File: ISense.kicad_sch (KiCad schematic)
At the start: 9 parts, among them U8 INA241A2xDDF

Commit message: added license and almost ready for prod
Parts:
- C46: Rating (none) -> 6.3V
- C48, C50, C52: Rating (none) -> 100V
- C49: Rating (none) -> 5V
- R22, R27: Rating (none) -> 100mW
- R23: Rating (none) -> 6W
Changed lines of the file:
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@@
+			)
+		)
+		(property "Rating" "6.3V"
+			(at 81.28 83.82 0)
+			(effects
+				(font
+					(size 1.27 1.27)
+				)
+				(hide yes)
 			)
 		)
@@
 			)
 		)
+		(property "Rating" "100V"
+			(at 99.06 62.23 0)
+			(effects
+				(font
+					(size 1.27 1.27)
+				)
+				(hide yes)
+			)
+		)
 		(pin "1"
 		)
@@
 			)
 		)
+		(property "Rating" "5V"
+			(at 106.68 62.23 0)
+			(effects
+				(font
+					(size 1.27 1.27)
+				)
+				(hide yes)
+			)
+		)
 		(pin "1"
 		)
@@
 			)
 		)
+		(property "Rating" "100mW"
+			(at 101.6 55.88 0)
+			(effects
+				(font
+					(size 1.27 1.27)
+				)
+				(hide yes)
+			)
+		)
 		(pin "1"
 		)
@@
 		)
 		(property "Description" "Unpolarized capacitor, small symbol"
+			(at 114.3 62.23 0)
+			(effects
+				(font
+					(size 1.27 1.27)
+				)
+				(hide yes)
+			)
+		)
+		(property "Rating" "100V"
 			(at 114.3 62.23 0)
 			(effects
@@
 			)
 		)
+		(property "Rating" "100V"
+			(at 87.63 83.82 0)
+			(effects
+				(font
+					(size 1.27 1.27)
+				)
+				(hide yes)
+			)
+		)
 		(pin "1"
 		)
@@
 			)
 		)
+		(property "Rating" "6W"
+			(at 106.68 40.64 0)
+			(effects
+				(font
+					(size 1.27 1.27)
+				)
+				(hide yes)
+			)
+		)
 		(pin "2"
 		)
@@
 			)
 		)
+		(property "Rating" "100mW"
+			(at 111.76 55.88 0)
+			(effects
+				(font
+					(size 1.27 1.27)
+				)
+				(hide yes)
+			)
+		)
 		(pin "1"
 		)
@@
 			(at 106.68 81.28 0)
 			(effects
+				(font
+					(size 1.27 1.27)
+				)
+				(hide yes)
+			)
+		)
+		(property "Rating" ""
+			(at 106.68 81.28 0)
+			(effects

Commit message: first fab run
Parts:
- removed C46: 4.7uF, Capacitor_SMD:C_0603_1608Metric, symbol Device:C_Small
- added C4: 4.7uF, Capacitor_SMD:C_0603_1608Metric, symbol Device:C
- C48, C50: Manufacturer_Part_Number (none) -> CGA0603X7R104K101JT; Source (none) -> LCSC
- C49: Manufacturer_Part_Number (none) -> CSA0603X7R103K500JT; Source (none) -> LCSC
- C52: Manufacturer_Part_Number (none) -> CGA0603X7R104K500JT; Rating 100V -> 6.3V; Source (none) -> LCSC
- R22, R27: Manufacturer_Part_Number (none) -> RTT0310R0FTP; Source (none) -> LCSC
- R23: Manufacturer_Part_Number (none) -> ASR-M-3-0.5F; Source (none) -> LCSC
- U8: value INA241A2xDDF -> INA240A2; footprint Package_TO_SOT_SMD:SOT-23-8 -> Package_SO:SO-8_3.9x4.9mm_P1.27mm; Manufacturer_Part_Number (none) -> INA240A2DR; Rating (none) -> 80V; Source (none) -> LCSC
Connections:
- net GND: now also C4.2
- net V_{DDA}: now also C4.1
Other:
- note added: "Common Mode Low Pass at 16kHz"
- note added: "Current Sense Shunt Resistor"
- note added: "Differential Low Pass at 800 kHz"
- note added: "I_{MAX} = 66A, I_{MIN} = -66A, V_{DDA} = 3.3V"
- note added: "V_{SENSE} = V_{DDA}/2 + I_{SHUNT} * .025"

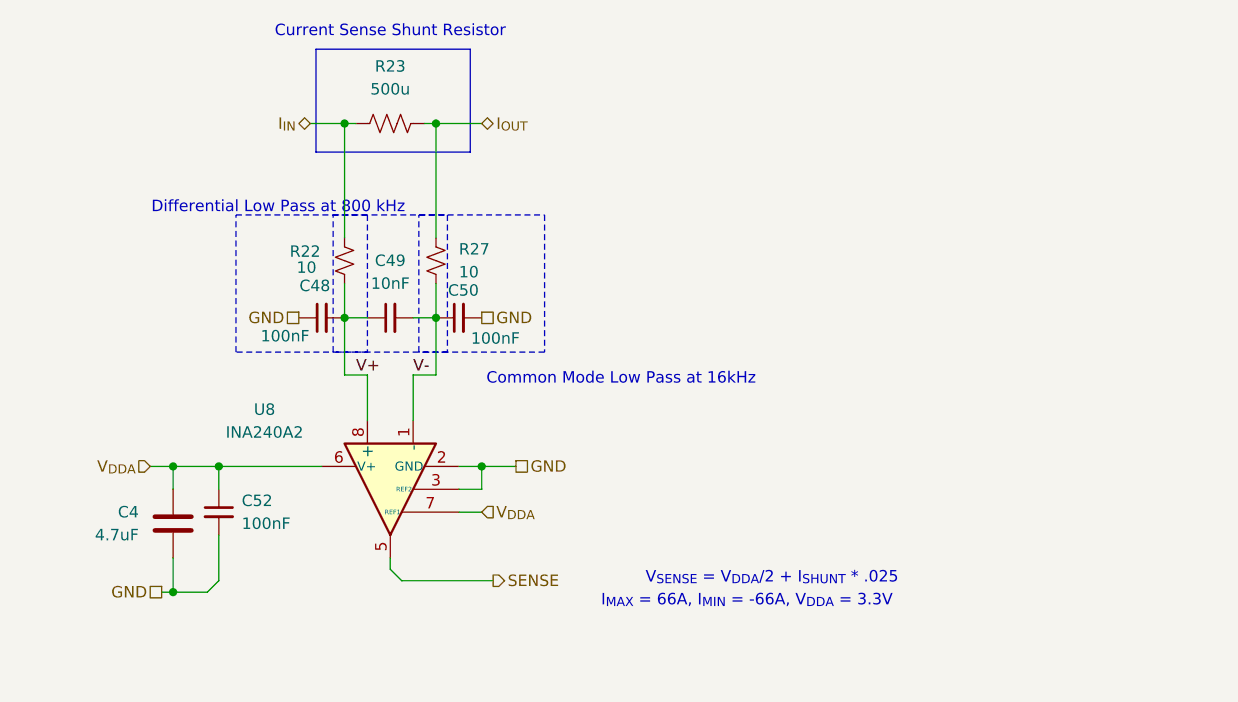
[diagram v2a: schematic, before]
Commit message: added ESD protection
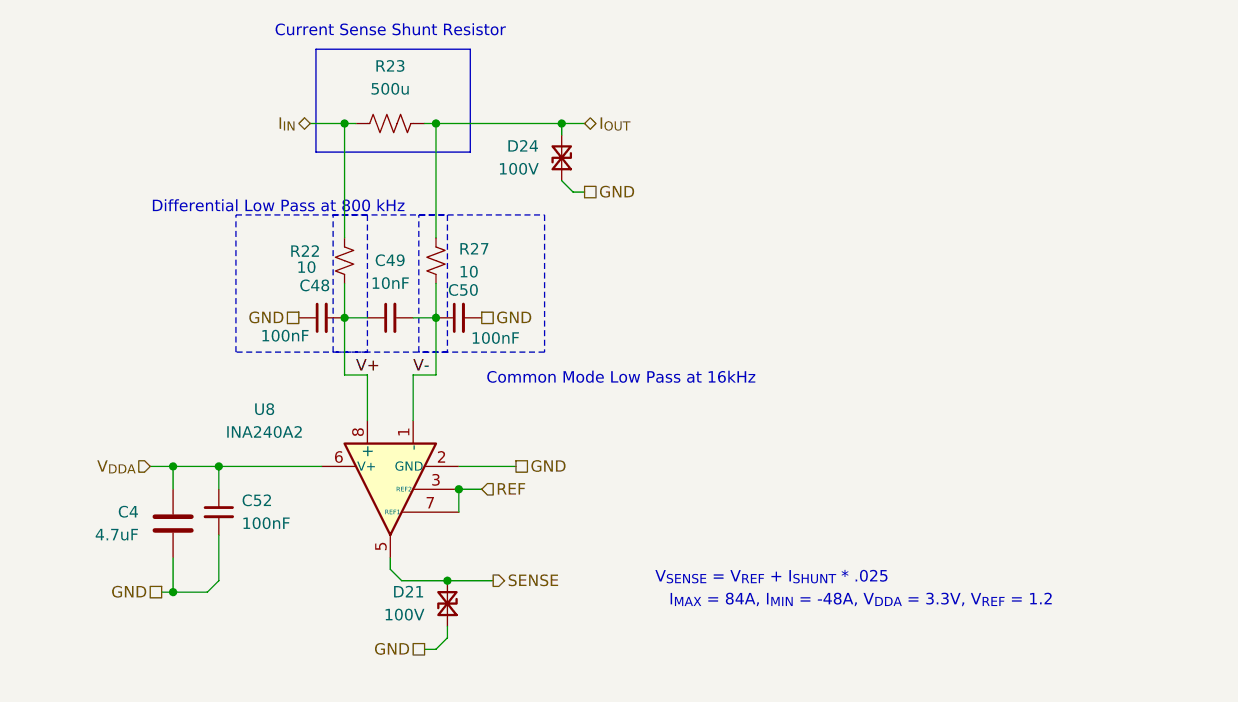
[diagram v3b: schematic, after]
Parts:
- added D21, D24: 100V, Diode_SMD:D_0603_1608Metric, symbol Device:D_TVS_Small
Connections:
- net GND: now also D21.1 (A1), D24.1 (A1); no longer U8.3 (REF2)
- net I_{OUT}: now also D24.2 (A2)
- net SENSE: now also D21.2 (A2)
- net V_{DDA}: no longer U8.7 (REF1)
- new net REF: U8.3 (REF2), U8.7 (REF1)
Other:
- note added: "I_{MAX} = 84A, I_{MIN} = -48A, V_{DDA} = 3.3V, V_{REF} = 1.2"
- note added: "V_{SENSE} = V_{REF} + I_{SHUNT} * .025"
- note removed: "I_{MAX} = 66A, I_{MIN} = -66A, V_{DDA} = 3.3V"
- note removed: "V_{SENSE} = V_{DDA}/2 + I_{SHUNT} * .025"

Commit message: add context
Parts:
- R23: value 500u -> .3m; Rating 6W -> 3W
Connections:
- net GND: now also U8.3 (REF2)
- net V_{DDA}: now also U8.7 (REF1)
- removed net REF: U8.3 (REF2), U8.7 (REF1)
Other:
- note added: "Gain = 50"
- note added: "I_{MAX} = 110A, I_{MIN} = -110A, V_{DDA} = 3.3V, V_{REF} = 1.65"
- note added: "V_{SENSE} = V_{REF} + I_{SHUNT} * .015"
- note removed: "I_{MAX} = 84A, I_{MIN} = -48A, V_{DDA} = 3.3V, V_{REF} = 1.2"
- note removed: "V_{SENSE} = V_{REF} + I_{SHUNT} * .025"
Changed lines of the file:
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@@
-	)
-	(junction
-		(at 114.3 81.28)
-		(diameter 0)
-		(color 0 0 0 0)
 	)
 	(junction
@@
 		(color 0 0 0 0)
 	)
+	(junction
+		(at 115.57 78.74)
+		(diameter 0)
+		(color 0 0 0 0)
+	)
 	(wire
 		(pts
@@
 	(wire
 		(pts
-			(xy 114.3 81.28) (xy 116.84 81.28)
-		)
-		(stroke
-			(width 0)
-			(type default)
-		)
-	)
-	(wire
-		(pts
 			(xy 101.6 62.23) (xy 101.6 68.58)
 		)
@@
 	(wire
 		(pts
-			(xy 114.3 81.28) (xy 114.3 83.82)
-		)
-		(stroke
-			(width 0)
-			(type default)
-		)
-	)
-	(wire
-		(pts
 			(xy 97.79 40.64) (xy 101.6 40.64)
 		)
@@
 	(wire
 		(pts
+			(xy 115.57 78.74) (xy 115.57 81.28)
+		)
+		(stroke
+			(width 0)
+			(type default)
+		)
+	)
+	(wire
+		(pts
 			(xy 87.63 78.74) (xy 87.63 81.28)
 		)
@@
 	(wire
 		(pts
+			(xy 115.57 78.74) (xy 120.65 78.74)
+		)
+		(stroke
+			(width 0)
+			(type default)
+		)
+	)
+	(wire
+		(pts
+			(xy 114.3 81.28) (xy 115.57 81.28)
+		)
+		(stroke
+			(width 0)
+			(type default)
+		)
+	)
+	(wire
+		(pts
 			(xy 87.63 86.36) (xy 87.63 91.44)
 		)
@@
 	(wire
 		(pts
-			(xy 114.3 78.74) (xy 120.65 78.74)
+			(xy 114.3 78.74) (xy 115.57 78.74)
 		)
 		(stroke
@@
 		)
 	)
-	(text "V_{SENSE} = V_{REF} + I_{SHUNT} * .025"
+	(text "V_{SENSE} = V_{REF} + I_{SHUNT} * .015"
 		(exclude_from_sim no)
 		(at 149.098 91.186 0)
@@
 		)
 	)
-	(text "I_{MAX} = 84A, I_{MIN} = -48A, V_{DDA} = 3.3V, V_{REF} = 1.2"
+	(text "Gain = 50\n"
+		(exclude_from_sim no)
+		(at 115.824 74.168 0)
+		(effects
+			(font
+				(size 1.27 1.27)
+			)
+		)
+	)
+	(text "I_{MAX} = 110A, I_{MIN} = -110A, V_{DDA} = 3.3V, V_{REF} = 1.65"
 		(exclude_from_sim no)
 		(at 159.004 93.726 0)
@@
 		)
 	)
+	(hierarchical_label "V_{DDA}"
+		(shape input)
+		(at 114.3 83.82 0)
+		(fields_autoplaced yes)
+		(effects
+			(font
+				(size 1.27 1.27)
+			)
+			(justify left)
+		)
+	)
 	(hierarchical_label "I_{IN}"
 		(shape bidirectional)
@@
 		(shape output)
 		(at 118.11 91.44 0)
-		(fields_autoplaced yes)
-		(effects
-			(font
-				(size 1.27 1.27)
-			)
-			(justify left)
-		)
-	)
-	(hierarchical_label "REF"
-		(shape input)
-		(at 116.84 81.28 0)
 		(fields_autoplaced yes)
 		(effects
@@
 			)
 		)
-		(property "Value" "500u"
+		(property "Value" ".3m"
 			(at 106.68 36.83 90)
 			(effects
@@
 			)
 		)
-		(property "Rating" "6W"
+		(property "Rating" "3W"
 			(at 106.68 40.64 0)
 			(effects

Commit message: adjusted according to Reddit feedback
Still needs TVS adjusted
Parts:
- U8: value INA240A2 -> INA241A2; footprint Package_SO:SO-8_3.9x4.9mm_P1.27mm -> Package_TO_SOT_SMD:SOT-23-8; Manufacturer_Part_Number INA240A2DR -> INA241A2DDFR; Rating 80V -> 110V
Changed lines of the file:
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@@
 		(instances
 			(project "OpenMD"
+				(path "/28611c8e-7644-4a1a-8c07-dc86cafc8f6c/2a00e860-f835-428e-8d60-1f81dad8d039/333c1edc-8103-4690-800d-12fcc828edaf"
+					(reference "C47")
+					(unit 1)
+				)
 				(path "/28611c8e-7644-4a1a-8c07-dc86cafc8f6c/2a00e860-f835-428e-8d60-1f81dad8d039/7e19f11a-277e-4650-9782-9c7c2d21b0fd"
 					(reference "C52")
@@
 				(path "/28611c8e-7644-4a1a-8c07-dc86cafc8f6c/2a00e860-f835-428e-8d60-1f81dad8d039/c7f7d708-2dea-4049-a8c4-f9d7592eff53"
 					(reference "C57")
-					(unit 1)
-				)
-				(path "/28611c8e-7644-4a1a-8c07-dc86cafc8f6c/2a00e860-f835-428e-8d60-1f81dad8d039/333c1edc-8103-4690-800d-12fcc828edaf"
-					(reference "C47")
 					(unit 1)
 				)
@@
 		(instances
 			(project "OpenMD"
+				(path "/28611c8e-7644-4a1a-8c07-dc86cafc8f6c/2a00e860-f835-428e-8d60-1f81dad8d039/333c1edc-8103-4690-800d-12fcc828edaf"
+					(reference "R24")
+					(unit 1)
+				)
 				(path "/28611c8e-7644-4a1a-8c07-dc86cafc8f6c/2a00e860-f835-428e-8d60-1f81dad8d039/7e19f11a-277e-4650-9782-9c7c2d21b0fd"
 					(reference "R27")
@@
 				(path "/28611c8e-7644-4a1a-8c07-dc86cafc8f6c/2a00e860-f835-428e-8d60-1f81dad8d039/c7f7d708-2dea-4049-a8c4-f9d7592eff53"
 					(reference "R30")
-					(unit 1)
-				)
-				(path "/28611c8e-7644-4a1a-8c07-dc86cafc8f6c/2a00e860-f835-428e-8d60-1f81dad8d039/333c1edc-8103-4690-800d-12fcc828edaf"
-					(reference "R24")
 					(unit 1)
 				)
@@
 			)
 		)
-		(property "Value" "INA240A2"
+		(property "Value" "INA241A2"
 			(at 92.71 74.9614 90)
 			(effects
@@
 			)
 		)
-		(property "Footprint" "Package_SO:SO-8_3.9x4.9mm_P1.27mm"
+		(property "Footprint" "Package_TO_SOT_SMD:SOT-23-8"
 			(at 123.19 81.28 0)
 			(effects
@@
 			)
 		)
-		(property "Rating" "80V"
+		(property "Rating" "110V"
 			(at 106.68 81.28 0)
 			(effects
@@
 			)
 		)
-		(property "Manufacturer_Part_Number" "INA240A2DR"
-			(at 106.68 81.28 0)
-			(effects
+		(property "Manufacturer_Part_Number" "INA241A2DDFR"
+			(at 106.68 81.28 0)
+			(effects

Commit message: added all changes from Reddit
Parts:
- removed D21: 100V, Diode_SMD:D_0603_1608Metric, symbol Device:D_TVS_Small
- added D21: 3.6V, Diode_SMD:D_SOD-323, symbol Device:D_Zener_Filled
- renumbered C52 to C47, R27 to R24
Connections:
- net GND: now also D21.2 (A)
- net SENSE: now also D21.1 (K)
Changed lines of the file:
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@@
+	)
+	(junction
+		(at 115.57 91.44)
+		(diameter 0)
+		(color 0 0 0 0)
 	)
 	(junction
@@
 	)
 	(junction
-		(at 113.03 91.44)
-		(diameter 0)
-		(color 0 0 0 0)
-	)
-	(junction
 		(at 101.6 62.23)
 		(diameter 0)
@@
 	(wire
 		(pts
+			(xy 115.57 91.44) (xy 118.11 91.44)
+		)
+		(stroke
+			(width 0)
+			(type default)
+		)
+	)
+	(wire
+		(pts
 			(xy 106.68 90.17) (xy 107.95 91.44)
 		)
@@
 	(wire
 		(pts
-			(xy 107.95 91.44) (xy 113.03 91.44)
-		)
-		(stroke
-			(width 0)
-			(type default)
-		)
-	)
-	(wire
-		(pts
 			(xy 101.6 40.64) (xy 101.6 53.34)
 		)
@@
 	(wire
 		(pts
-			(xy 113.03 91.44) (xy 118.11 91.44)
+			(xy 107.95 91.44) (xy 115.57 91.44)
 		)
 		(stroke
@@
 	(wire
 		(pts
-			(xy 111.76 99.06) (xy 113.03 97.79)
-		)
-		(stroke
-			(width 0)
-			(type default)
-		)
-	)
-	(wire
-		(pts
-			(xy 113.03 96.52) (xy 113.03 97.79)
+			(xy 114.3 101.6) (xy 115.57 100.33)
+		)
+		(stroke
+			(width 0)
+			(type default)
+		)
+	)
+	(wire
+		(pts
+			(xy 115.57 99.06) (xy 115.57 100.33)
 		)
 		(stroke
@@
 	(wire
 		(pts
-			(xy 110.49 99.06) (xy 111.76 99.06)
+			(xy 113.03 101.6) (xy 114.3 101.6)
 		)
 		(stroke
@@
 	(hierarchical_label "GND"
 		(shape passive)
-		(at 110.49 99.06 180)
+		(at 113.03 101.6 180)
 		(fields_autoplaced yes)
 		(effects
@@
 	)
 	(symbol
+		(lib_id "Device:D_Zener_Filled")
+		(at 115.57 95.25 90)
+		(mirror x)
+		(unit 1)
+		(exclude_from_sim no)
+		(in_bom yes)
+		(on_board yes)
+		(dnp no)
+		(property "Reference" "D21"
+			(at 122.428 93.98 90)
+			(effects
+				(font
+					(size 1.27 1.27)
+				)
+				(justify left)
+			)
+		)
+		(property "Value" "3.6V"
+			(at 122.936 96.012 90)
+			(effects
+				(font
+					(size 1.27 1.27)
+				)
+				(justify left)
+			)
+		)
+		(property "Footprint" "Diode_SMD:D_SOD-323"
+			(at 115.57 95.25 0)
+			(effects
+				(font
+					(size 1.27 1.27)
+				)
+				(hide yes)
+			)
+		)
+		(property "Datasheet" "~"
+			(at 115.57 95.25 0)
+			(effects
+				(font
+					(size 1.27 1.27)
+				)
+				(hide yes)
+			)
+		)
+		(property "Description" "Zener diode, filled shape"
+			(at 115.57 95.25 0)
+			(effects
+				(font
+					(size 1.27 1.27)
+				)
+				(hide yes)
+			)
+		)
+		(property "Rating" "1A"
+			(at 115.57 95.25 0)
+			(effects
+				(font
+					(size 1.27 1.27)
+				)
+				(hide yes)
+			)
+		)
+		(property "Manufacturer_Part_Number" "BZT52C3V3S"
+			(at 115.57 95.25 0)
+			(effects
+				(font
+					(size 1.27 1.27)
+				)
+				(hide yes)
+			)
+		)
+		(property "Source" "LCSC"
+			(at 115.57 95.25 0)
+			(effects
+				(font
+					(size 1.27 1.27)
+				)
+				(hide yes)
+			)
+		)
+		(pin "1"
+		)
+		(pin "2"
+		)
+		(instances
+			(project "OpenMD"
+				(path "/28611c8e-7644-4a1a-8c07-dc86cafc8f6c/2a00e860-f835-428e-8d60-1f81dad8d039/333c1edc-8103-4690-800d-12fcc828edaf"
+					(reference "D21")
+					(unit 1)
+				)
+				(path "/28611c8e-7644-4a1a-8c07-dc86cafc8f6c/2a00e860-f835-428e-8d60-1f81dad8d039/7e19f11a-277e-4650-9782-9c7c2d21b0fd"
+					(reference "D22")
+					(unit 1)
+				)
+				(path "/28611c8e-7644-4a1a-8c07-dc86cafc8f6c/2a00e860-f835-428e-8d60-1f81dad8d039/c7f7d708-2dea-4049-a8c4-f9d7592eff53"
+					(reference "D23")
+					(unit 1)
+				)
+			)
+		)
+	)
+	(symbol
 		(lib_id "Device:C_Small")
 		(at 99.06 62.23 90)
@@
 	)
 	(symbol
-		(lib_id "Device:D_TVS_Small")
-		(at 113.03 93.98 270)
-		(mirror x)
-		(unit 1)
-		(exclude_from_sim no)
-		(in_bom yes)
-		(on_board yes)
-		(dnp no)
-		(property "Reference" "D21"
-			(at 110.49 92.7099 90)
-			(effects
-				(font
-					(size 1.27 1.27)
-				)
-				(justify right)
-			)
-		)
-		(property "Value" "100V"
-			(at 110.49 95.2499 90)
-			(effects
-				(font
-					(size 1.27 1.27)
-				)
-				(justify right)
-			)
-		)
-		(property "Footprint" "Diode_SMD:D_0603_1608Metric"
-			(at 113.03 93.98 0)
-			(effects
-				(font
-					(size 1.27 1.27)
-				)
-				(hide yes)
-			)
-		)
-		(property "Datasheet" "~"
-			(at 113.03 93.98 0)
-			(effects
-				(font
-					(size 1.27 1.27)
-				)
-				(hide yes)
-			)
-		)
-		(property "Description" "Bidirectional transient-voltage-suppression diode, small symbol"
-			(at 113.03 93.98 0)
-			(effects
-				(font
-					(size 1.27 1.27)
-				)
-				(hide yes)
-			)
-		)
-		(property "Manufacturer_Part_Number" "ULCE1005A015FR"
-			(at 113.03 93.98 0)
-			(effects
-				(font
-					(size 1.27 1.27)
-				)
-				(hide yes)
-			)
-		)
-		(property "Source" "LCSC"
-			(at 113.03 93.98 0)
-			(effects
-				(font
-					(size 1.27 1.27)
-				)
-				(hide yes)
-			)
-		)
-		(property "Rating" "1A"
-			(at 113.03 93.98 0)
-			(effects
-				(font
-					(size 1.27 1.27)
-				)
-				(hide yes)
-			)
-		)
-		(pin "2"
-		)
-		(pin "1"
-		)
-		(instances
-			(project "OpenMD"
-				(path "/28611c8e-7644-4a1a-8c07-dc86cafc8f6c/2a00e860-f835-428e-8d60-1f81dad8d039/333c1edc-8103-4690-800d-12fcc828edaf"
-					(reference "D21")
-					(unit 1)
-				)
-				(path "/28611c8e-7644-4a1a-8c07-dc86cafc8f6c/2a00e860-f835-428e-8d60-1f81dad8d039/7e19f11a-277e-4650-9782-9c7c2d21b0fd"
-					(reference "D22")
-					(unit 1)
-				)
-				(path "/28611c8e-7644-4a1a-8c07-dc86cafc8f6c/2a00e860-f835-428e-8d60-1f81dad8d039/c7f7d708-2dea-4049-a8c4-f9d7592eff53"
-					(reference "D23")
-					(unit 1)
-				)
-			)
-		)
-	)
-	(symbol
 		(lib_id "Device:C_Small")
 		(at 114.3 62.23 90)
@@
 		(dnp no)
 		(fields_autoplaced yes)
-		(property "Reference" "C52"
+		(property "Reference" "C47"
 			(at 90.17 82.5562 0)
 			(effects
@@
 		(dnp no)
 		(fields_autoplaced yes)
-		(property "Reference" "R27"
+		(property "Reference" "R24"
 			(at 114.3 54.6099 0)
 			(effects

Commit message: updates to make better
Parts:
- D21: value 3.6V -> 3.3V
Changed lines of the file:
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@@
 			)
 		)
-		(property "Value" "3.6V"
+		(property "Value" "3.3V"
 			(at 122.936 96.012 90)
 			(effects

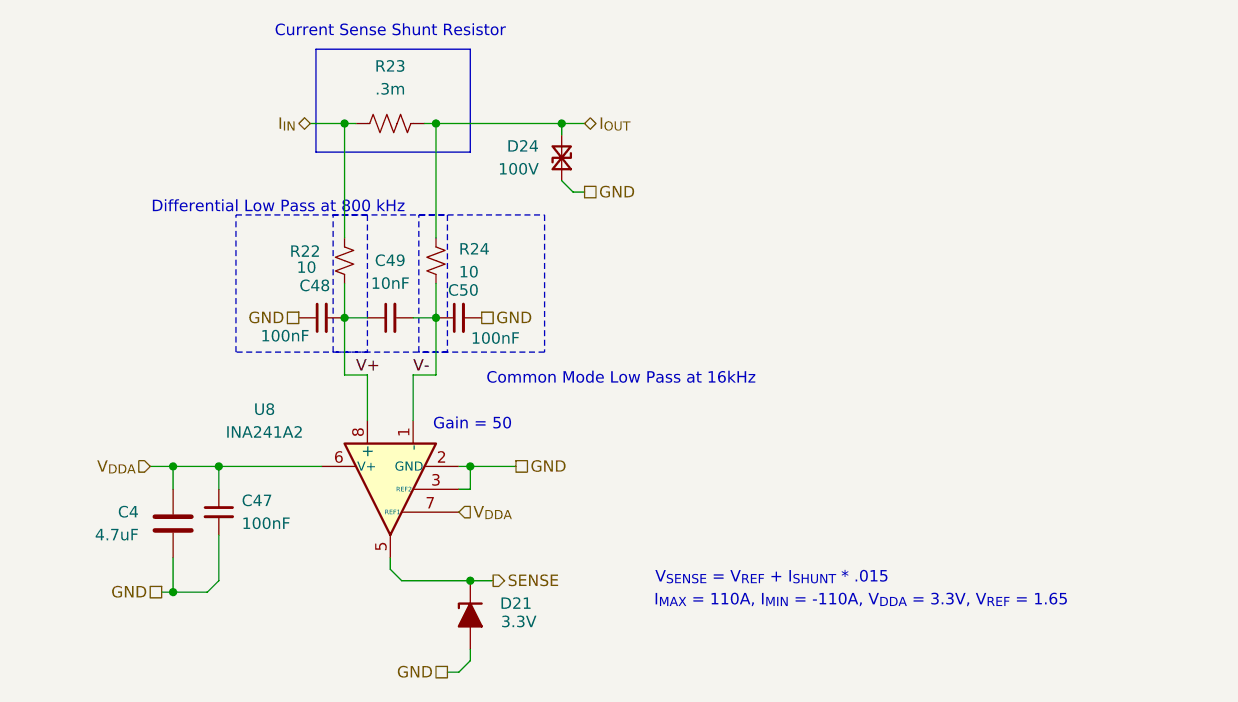
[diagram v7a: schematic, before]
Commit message: moved amps to back
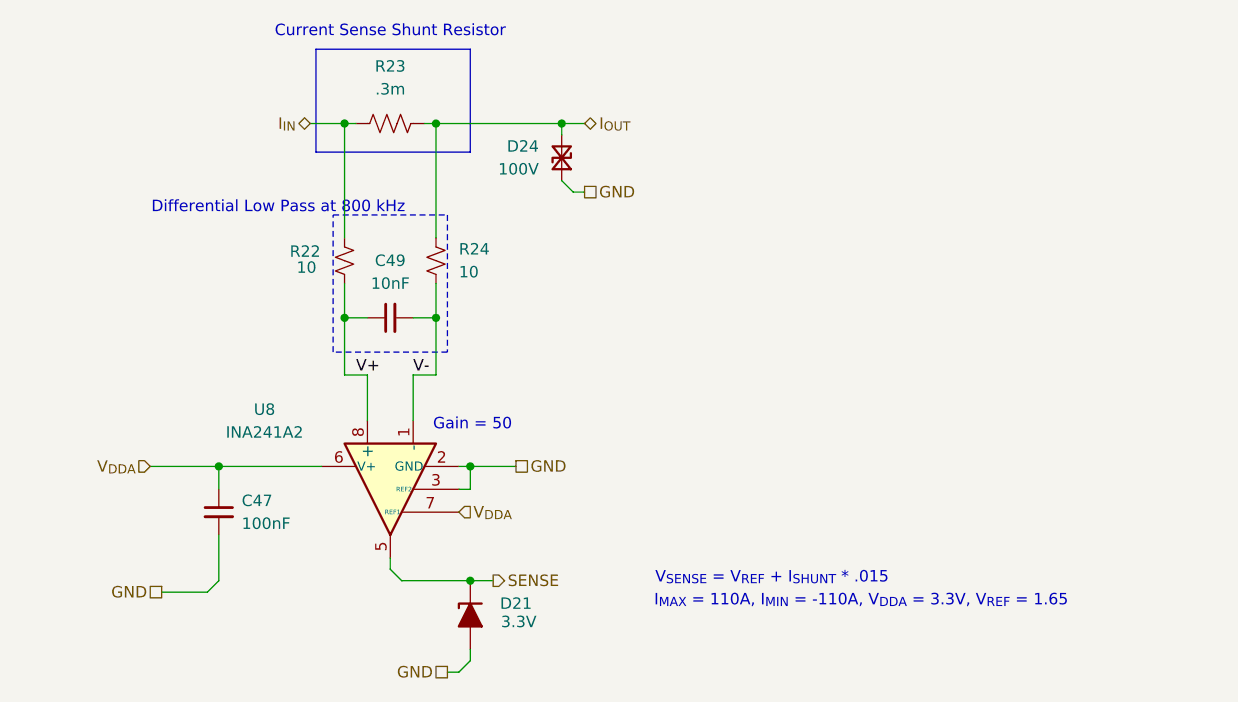
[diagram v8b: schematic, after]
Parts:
- removed C4: 4.7uF, Capacitor_SMD:C_0603_1608Metric, symbol Device:C
- removed C48, C50: 100nF, Capacitor_SMD:C_0603_1608Metric, symbol Device:C_Small
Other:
- note removed: "Common Mode Low Pass at 16kHz"
